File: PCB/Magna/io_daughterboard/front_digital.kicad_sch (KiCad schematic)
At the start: 67 parts, among them U1801 XL9535

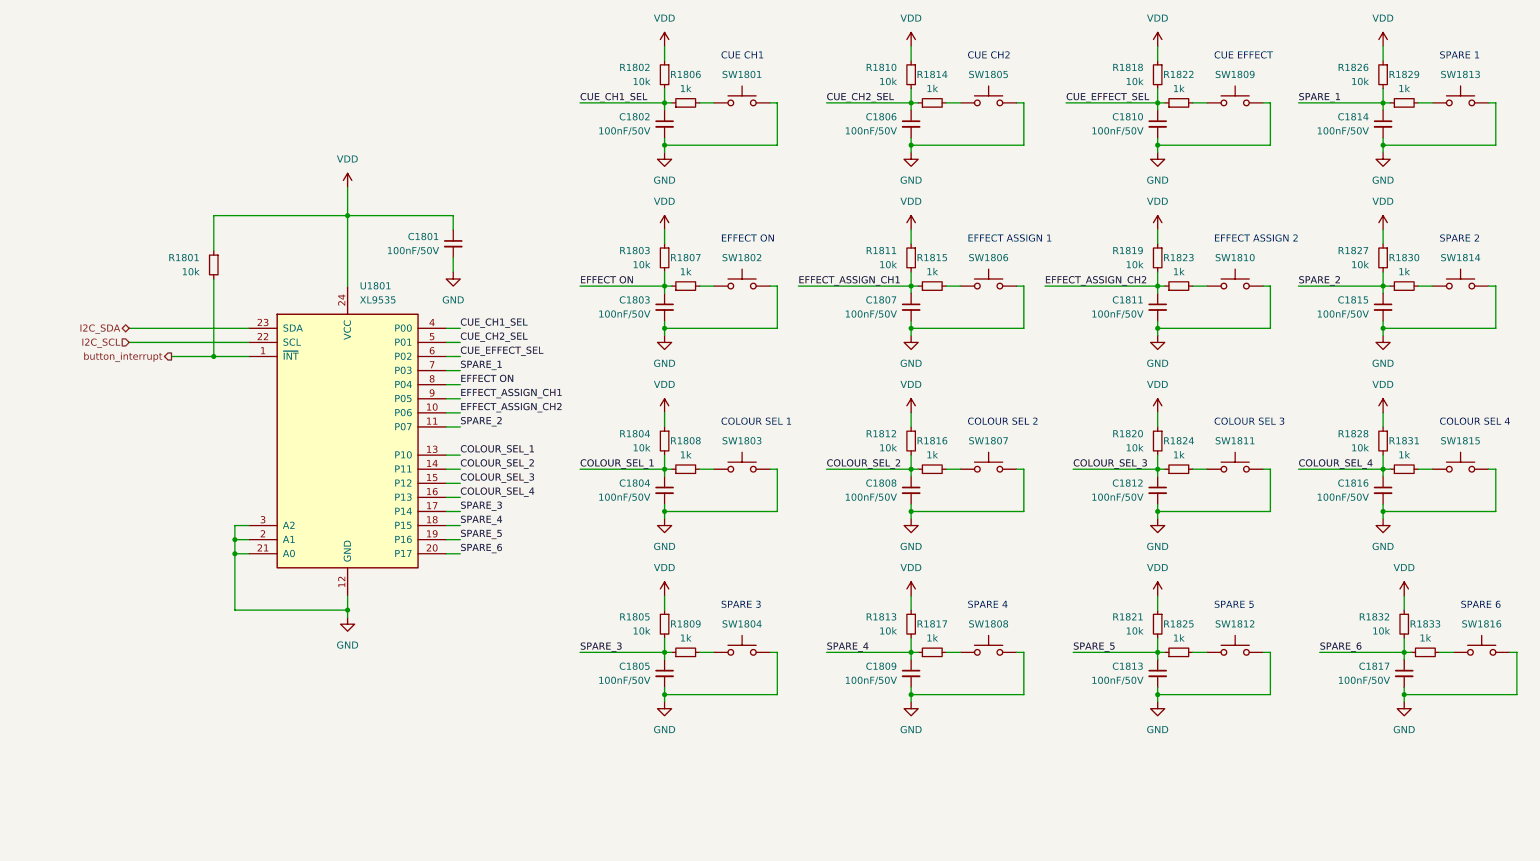
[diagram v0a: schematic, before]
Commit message: Split schematic to several projects
To allow for several boards to be done a kicad project
is needed for each
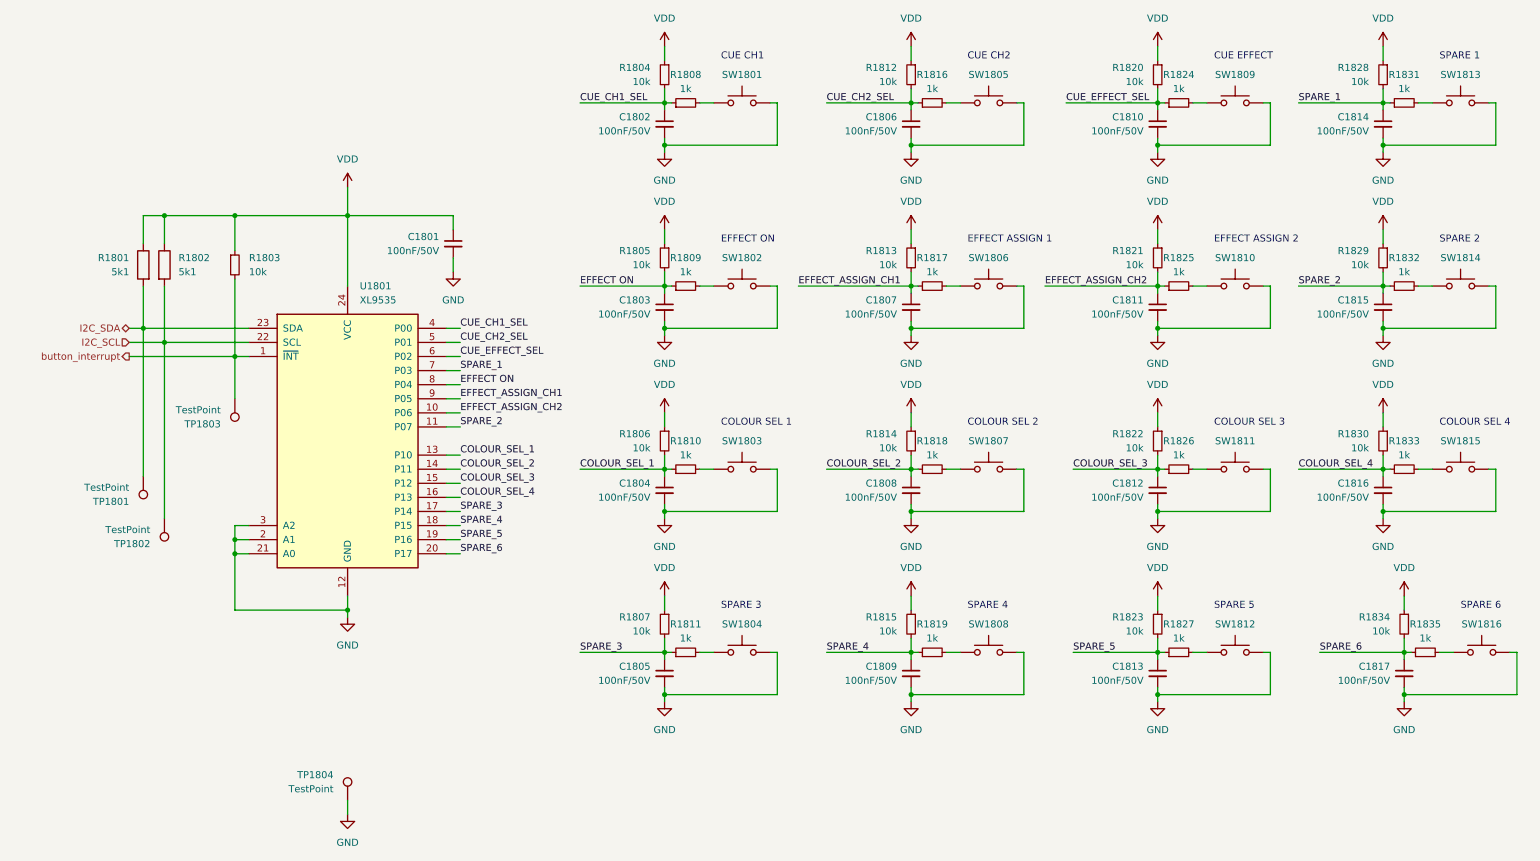
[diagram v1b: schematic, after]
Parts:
- added R1801, R1802: 5k1, Resistor_SMD:R_0805_2012Metric_Pad1.20x1.40mm_HandSolder, symbol Device:R
- added TP1801, TP1802, TP1803, TP1804: TestPoint, TestPoint:TestPoint_Keystone_5005-5009_Compact, symbol Connector:TestPoint
- renumbered R1801 to R1803, R1802 to R1804, R1803 to R1805, R1804 to R1806, R1805 to R1807, R1806 to R1808, R1807 to R1809, R1808 to R1810, R1809 to R1811, R1810 to R1812, R1811 to R1813, R1812 to R1814, R1813 to R1815, R1814 to R1816, R1815 to R1817, R1816 to R1818, R1817 to R1819, R1818 to R1820, R1819 to R1821, R1820 to R1822, R1821 to R1823, R1822 to R1824, R1823 to R1825, R1824 to R1826, R1825 to R1827, R1826 to R1828, R1827 to R1829, R1828 to R1830, R1829 to R1831, R1830 to R1832, R1831 to R1833, R1832 to R1834, R1833 to R1835
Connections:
- net GND: now also TP1804.1
- net I2C_SCL: now also R1802.2, TP1802.1
- net I2C_SDA: now also R1801.2, TP1801.1
- net VDD: now also R1801.1, R1802.1
- net button_interrupt: now also TP1803.1
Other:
- moved on the sheet: R1803

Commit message: Route most of io daughterboard
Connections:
- net COLOUR_SEL_1: no longer U1801.13 (P10)
- net COLOUR_SEL_2: now also U1801.18 (P15); no longer U1801.14 (P11)
- net COLOUR_SEL_3: now also U1801.19 (P16); no longer U1801.15 (P12)
- net COLOUR_SEL_4: now also U1801.20 (P17); no longer U1801.16 (P13)
- net CUE_CH1_SEL: no longer U1801.4 (P00)
- net CUE_CH2_SEL: now also U1801.15 (P12); no longer U1801.5 (P01)
- net CUE_EFFECT_SEL: now also U1801.10 (P06); no longer U1801.6 (P02)
- net EFFECT ON: now also U1801.4 (P00); no longer U1801.8 (P04)
- net EFFECT_ASSIGN_CH1: now also U1801.13 (P10); no longer U1801.9 (P05)
- net EFFECT_ASSIGN_CH2: now also U1801.14 (P11); no longer U1801.10 (P06)
- net SPARE_1: now also U1801.11 (P07); no longer U1801.7 (P03)
- net SPARE_2: now also U1801.9 (P05); no longer U1801.11 (P07)
- net SPARE_3: now also U1801.5 (P01); no longer U1801.17 (P14)
- net SPARE_4: now also U1801.6 (P02); no longer U1801.18 (P15)
- net SPARE_5: now also U1801.7 (P03); no longer U1801.19 (P16)
- net SPARE_6: now also U1801.8 (P04); no longer U1801.20 (P17)
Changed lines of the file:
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@@
   (junction (at 165.1 81.28) (diameter 0) (color 0 0 0 0)
   )
+  (junction (at 120.65 48.26) (diameter 0) (color 0 0 0 0)
+  )
   (junction (at 63.5 60.96) (diameter 0) (color 0 0 0 0)
   )
@@
   (junction (at 209.55 48.26) (diameter 0) (color 0 0 0 0)
   )
-  (junction (at 120.65 48.26) (diameter 0) (color 0 0 0 0)
-  )
   (junction (at 120.65 139.7) (diameter 0) (color 0 0 0 0)
   )
@@
     (stroke (width 0) (type default))
   )
+  (wire (pts (xy 120.65 48.26) (xy 120.65 49.53))
+    (stroke (width 0) (type default))
+  )
   (wire (pts (xy 81.28 104.14) (xy 83.82 104.14))
     (stroke (width 0) (type default))
@@
     (stroke (width 0) (type default))
   )
+  (wire (pts (xy 140.97 48.26) (xy 120.65 48.26))
+    (stroke (width 0) (type default))
+  )
   (wire (pts (xy 234.95 73.66) (xy 250.19 73.66))
     (stroke (width 0) (type default))
@@
     (stroke (width 0) (type default))
   )
-  (wire (pts (xy 140.97 48.26) (xy 140.97 40.64))
-    (stroke (width 0) (type default))
-  )
   (wire (pts (xy 120.65 147.32) (xy 140.97 147.32))
     (stroke (width 0) (type default))
@@
     (stroke (width 0) (type default))
   )
-  (wire (pts (xy 120.65 48.26) (xy 140.97 48.26))
-    (stroke (width 0) (type default))
-  )
   (wire (pts (xy 209.55 114.3) (xy 209.55 115.57))
     (stroke (width 0) (type default))
@@
     (stroke (width 0) (type default))
   )
-  (wire (pts (xy 105.41 40.64) (xy 120.65 40.64))
+  (wire (pts (xy 97.79 40.64) (xy 120.65 40.64))
     (stroke (width 0) (type default))
   )
@@
     (stroke (width 0) (type default))
   )
+  (wire (pts (xy 140.97 40.64) (xy 140.97 48.26))
+    (stroke (width 0) (type default))
+  )
   (wire (pts (xy 166.37 73.66) (xy 165.1 73.66))
     (stroke (width 0) (type default))
@@
     (stroke (width 0) (type default))
   )
-  (wire (pts (xy 120.65 48.26) (xy 120.65 49.53))
-    (stroke (width 0) (type default))
-  )
   (wire (pts (xy 81.28 119.38) (xy 83.82 119.38))
     (stroke (width 0) (type default))
@@
     (effects (font (size 1.27 1.27)) (justify left bottom))
   )
-  (label "EFFECT_ASSIGN_CH2" (at 83.82 96.52 0) (fields_autoplaced)
+  (label "EFFECT_ASSIGN_CH2" (at 83.82 106.68 0) (fields_autoplaced)
     (effects (font (size 1.27 1.27)) (justify left bottom))
   )
-  (label "SPARE_4" (at 83.82 116.84 0) (fields_autoplaced)
+  (label "SPARE_4" (at 83.82 86.36 0) (fields_autoplaced)
     (effects (font (size 1.27 1.27)) (justify left bottom))
   )
@@
     (effects (font (size 1.27 1.27)) (justify left bottom))
   )
-  (label "COLOUR_SEL_4" (at 83.82 111.76 0) (fields_autoplaced)
+  (label "COLOUR_SEL_4" (at 83.82 121.92 0) (fields_autoplaced)
     (effects (font (size 1.27 1.27)) (justify left bottom))
   )
@@
     (effects (font (size 1.27 1.27)) (justify left bottom))
   )
-  (label "SPARE_3" (at 83.82 114.3 0) (fields_autoplaced)
+  (label "SPARE_3" (at 83.82 83.82 0) (fields_autoplaced)
     (effects (font (size 1.27 1.27)) (justify left bottom))
   )
-  (label "CUE_CH2_SEL" (at 83.82 83.82 0) (fields_autoplaced)
+  (label "CUE_CH2_SEL" (at 83.82 109.22 0) (fields_autoplaced)
     (effects (font (size 1.27 1.27)) (justify left bottom))
   )
-  (label "CUE_EFFECT_SEL" (at 83.82 86.36 0) (fields_autoplaced)
+  (label "CUE_EFFECT_SEL" (at 83.82 96.52 0) (fields_autoplaced)
     (effects (font (size 1.27 1.27)) (justify left bottom))
   )
-  (label "EFFECT ON" (at 83.82 91.44 0) (fields_autoplaced)
+  (label "EFFECT ON" (at 83.82 81.28 0) (fields_autoplaced)
     (effects (font (size 1.27 1.27)) (justify left bottom))
   )
@@
     (effects (font (size 1.27 1.27)) (justify left bottom))
   )
-  (label "SPARE_6" (at 83.82 121.92 0) (fields_autoplaced)
+  (label "SPARE_6" (at 83.82 91.44 0) (fields_autoplaced)
     (effects (font (size 1.27 1.27)) (justify left bottom))
   )
@@
     (effects (font (size 1.27 1.27)) (justify left bottom))
   )
-  (label "COLOUR_SEL_1" (at 83.82 104.14 0) (fields_autoplaced)
+  (label "COLOUR_SEL_1" (at 86.36 135.255 0) (fields_autoplaced)
     (effects (font (size 1.27 1.27)) (justify left bottom))
   )
@@
     (effects (font (size 1.27 1.27)) (justify left bottom))
   )
-  (label "COLOUR_SEL_3" (at 83.82 109.22 0) (fields_autoplaced)
+  (label "COLOUR_SEL_3" (at 83.82 119.38 0) (fields_autoplaced)
     (effects (font (size 1.27 1.27)) (justify left bottom))
   )
-  (label "SPARE_1" (at 83.82 88.9 0) (fields_autoplaced)
+  (label "SPARE_1" (at 83.82 99.06 0) (fields_autoplaced)
     (effects (font (size 1.27 1.27)) (justify left bottom))
   )
@@
     (effects (font (size 1.27 1.27)) (justify left bottom))
   )
-  (label "CUE_CH1_SEL" (at 83.82 81.28 0) (fields_autoplaced)
+  (label "CUE_CH1_SEL" (at 90.805 65.405 0) (fields_autoplaced)
     (effects (font (size 1.27 1.27)) (justify left bottom))
   )
-  (label "EFFECT_ASSIGN_CH1" (at 83.82 93.98 0) (fields_autoplaced)
+  (label "EFFECT_ASSIGN_CH1" (at 83.82 104.14 0) (fields_autoplaced)
     (effects (font (size 1.27 1.27)) (justify left bottom))
   )
-  (label "CUE_CH1_SEL" (at 105.41 40.64 0) (fields_autoplaced)
+  (label "CUE_CH1_SEL" (at 97.79 40.64 0) (fields_autoplaced)
     (effects (font (size 1.27 1.27)) (justify left bottom))
   )
-  (label "SPARE_5" (at 83.82 119.38 0) (fields_autoplaced)
+  (label "SPARE_5" (at 83.82 88.9 0) (fields_autoplaced)
     (effects (font (size 1.27 1.27)) (justify left bottom))
   )
-  (label "COLOUR_SEL_2" (at 83.82 106.68 0) (fields_autoplaced)
+  (label "COLOUR_SEL_2" (at 83.82 116.84 0) (fields_autoplaced)
     (effects (font (size 1.27 1.27)) (justify left bottom))
   )
@@
     (effects (font (size 1.27 1.27)) (justify left bottom))
   )
-  (label "SPARE_2" (at 83.82 99.06 0) (fields_autoplaced)
+  (label "SPARE_2" (at 83.82 93.98 0) (fields_autoplaced)
     (effects (font (size 1.27 1.27)) (justify left bottom))
   )
@@
     )
   )
-  (symbol (lib_id "Device:C_Small") (at 120.65 44.45 0) (unit 1)
+  (symbol (lib_id "Device:C_Small") (at 120.65 44.45 0) (mirror y) (unit 1)
     (in_bom yes) (on_board yes) (dnp no)
-    (property "Reference" "C1802" (at 118.11 43.1863 0)
+    (property "Reference" "C1802" (at 123.19 43.1863 0)
       (effects (font (size 1.27 1.27)) (justify right))
     )
-    (property "Value" "100nF/50V" (at 118.11 45.7263 0)
+    (property "Value" "100nF/50V" (at 123.19 45.7263 0)
       (effects (font (size 1.27 1.27)) (justify right))
     )

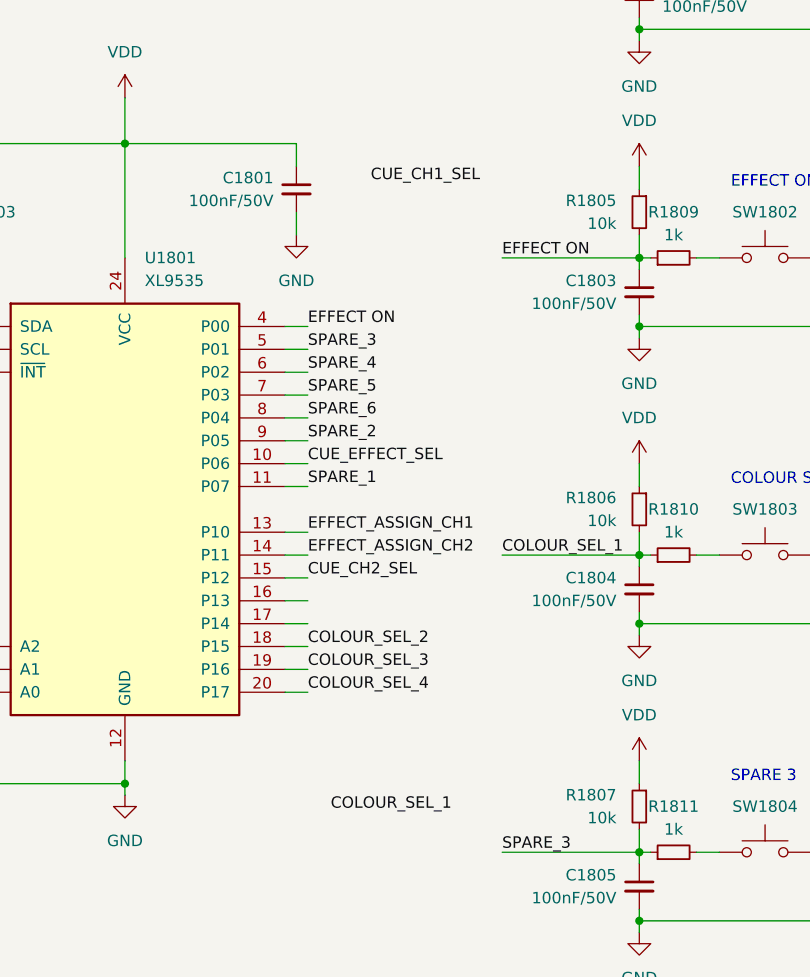
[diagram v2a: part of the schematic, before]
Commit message: Add more routing to IO Daugherboard
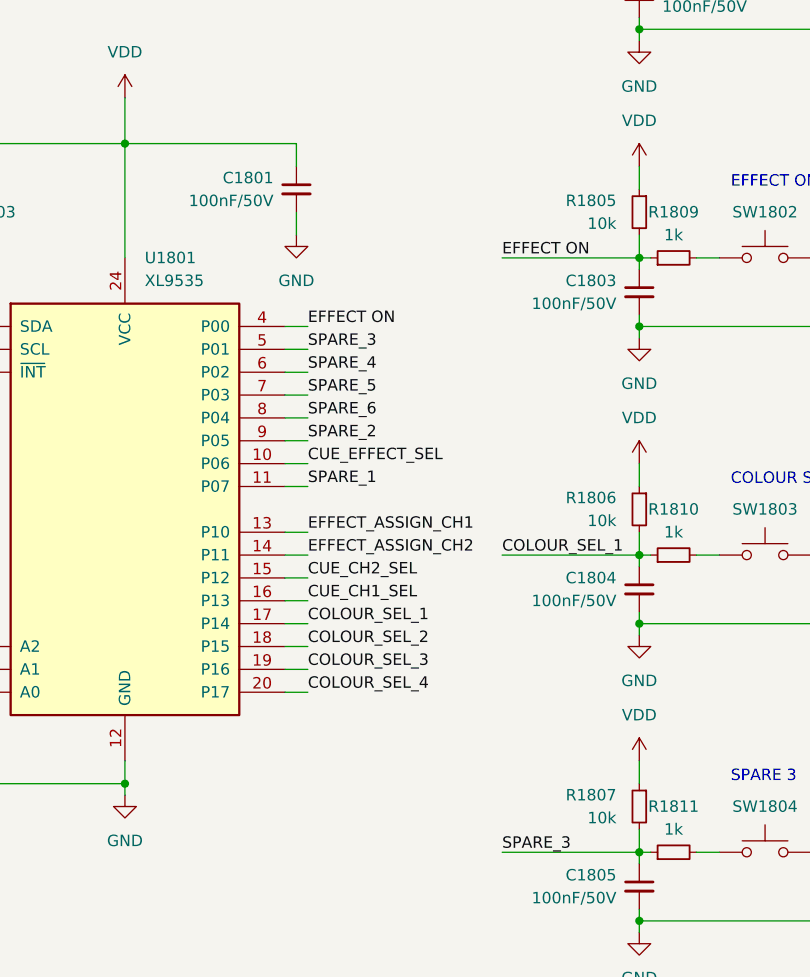
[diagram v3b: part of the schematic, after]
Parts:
- TP1801, TP1802, TP1803, TP1804: footprint TestPoint:TestPoint_Keystone_5005-5009_Compact -> TestPoint:TestPoint_Keystone_5000-5004_Miniature
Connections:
- net COLOUR_SEL_1: now also U1801.17 (P14)
- net CUE_CH1_SEL: now also U1801.16 (P13)
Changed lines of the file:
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@@
     (effects (font (size 1.27 1.27)) (justify left bottom))
   )
+  (label "COLOUR_SEL_1" (at 83.82 114.3 0) (fields_autoplaced)
+    (effects (font (size 1.27 1.27)) (justify left bottom))
+  )
   (label "SPARE_4" (at 149.86 139.7 0) (fields_autoplaced)
     (effects (font (size 1.27 1.27)) (justify left bottom))
@@
     (effects (font (size 1.27 1.27)) (justify left bottom))
   )
-  (label "COLOUR_SEL_1" (at 86.36 135.255 0) (fields_autoplaced)
-    (effects (font (size 1.27 1.27)) (justify left bottom))
-  )
   (label "SPARE_3" (at 105.41 139.7 0) (fields_autoplaced)
     (effects (font (size 1.27 1.27)) (justify left bottom))
@@
     (effects (font (size 1.27 1.27)) (justify left bottom))
   )
-  (label "CUE_CH1_SEL" (at 90.805 65.405 0) (fields_autoplaced)
+  (label "CUE_CH1_SEL" (at 83.82 111.76 0) (fields_autoplaced)
     (effects (font (size 1.27 1.27)) (justify left bottom))
   )
@@
       (effects (font (size 1.27 1.27)) (justify left))
     )
-    (property "Footprint" "TestPoint:TestPoint_Keystone_5005-5009_Compact" (at 21.59 107.95 0)
+    (property "Footprint" "TestPoint:TestPoint_Keystone_5000-5004_Miniature" (at 21.59 107.95 0)
       (effects (font (size 1.27 1.27)) hide)
     )
@@
       (effects (font (size 1.27 1.27)) (justify left))
     )
-    (property "Footprint" "TestPoint:TestPoint_Keystone_5005-5009_Compact" (at 25.4 115.57 0)
+    (property "Footprint" "TestPoint:TestPoint_Keystone_5000-5004_Miniature" (at 25.4 115.57 0)
       (effects (font (size 1.27 1.27)) hide)
     )
@@
       (effects (font (size 1.27 1.27)) (justify left))
     )
-    (property "Footprint" "TestPoint:TestPoint_Keystone_5005-5009_Compact" (at 38.1 93.98 0)
+    (property "Footprint" "TestPoint:TestPoint_Keystone_5000-5004_Miniature" (at 38.1 93.98 0)
       (effects (font (size 1.27 1.27)) hide)
     )
@@
       (effects (font (size 1.27 1.27)) (justify right))
     )
-    (property "Footprint" "TestPoint:TestPoint_Keystone_5005-5009_Compact" (at 68.58 166.37 0)
+    (property "Footprint" "TestPoint:TestPoint_Keystone_5000-5004_Miniature" (at 68.58 166.37 0)
       (effects (font (size 1.27 1.27)) hide)
     )

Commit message: Make IO daughterboard production ready
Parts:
- SW1801, SW1802, SW1803, SW1804, SW1805, SW1806, SW1807, SW1808, SW1809, SW1810, SW1811, SW1812, SW1813, SW1814, SW1815, SW1816: LCSC (none) -> C318884
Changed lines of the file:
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@@
+      (effects (font (size 1.27 1.27)) hide)
+    )
+    (property "LCSC" "C318884" (at 134.62 139.7 0)
       (effects (font (size 1.27 1.27)) hide)
     )
@@
       (effects (font (size 1.27 1.27)) hide)
     )
+    (property "LCSC" "C318884" (at 179.07 73.66 0)
+      (effects (font (size 1.27 1.27)) hide)
+    )
     (pin "2")
     (pin "1")
@@
     )
     (property "Datasheet" "~" (at 264.16 68.58 0)
+      (effects (font (size 1.27 1.27)) hide)
+    )
+    (property "LCSC" "C318884" (at 264.16 73.66 0)
       (effects (font (size 1.27 1.27)) hide)
     )
@@
       (effects (font (size 1.27 1.27)) hide)
     )
+    (property "LCSC" "C318884" (at 223.52 139.7 0)
+      (effects (font (size 1.27 1.27)) hide)
+    )
     (pin "2")
     (pin "1")
@@
     )
     (property "Datasheet" "~" (at 223.52 35.56 0)
+      (effects (font (size 1.27 1.27)) hide)
+    )
+    (property "LCSC" "C318884" (at 223.52 40.64 0)
       (effects (font (size 1.27 1.27)) hide)
     )
@@
       (effects (font (size 1.27 1.27)) hide)
     )
+    (property "LCSC" "C318884" (at 134.62 73.66 0)
+      (effects (font (size 1.27 1.27)) hide)
+    )
     (pin "2")
     (pin "1")
@@
     )
     (property "Datasheet" "~" (at 223.52 101.6 0)
+      (effects (font (size 1.27 1.27)) hide)
+    )
+    (property "LCSC" "C318884" (at 223.52 106.68 0)
       (effects (font (size 1.27 1.27)) hide)
     )
@@
       (effects (font (size 1.27 1.27)) hide)
     )
+    (property "LCSC" "C318884" (at 179.07 40.64 0)
+      (effects (font (size 1.27 1.27)) hide)
+    )
     (pin "2")
     (pin "1")
@@
       (effects (font (size 1.27 1.27)) hide)
     )
+    (property "LCSC" "C318884" (at 267.97 139.7 0)
+      (effects (font (size 1.27 1.27)) hide)
+    )
     (pin "2")
     (pin "1")
@@
       (effects (font (size 1.27 1.27)) hide)
     )
+    (property "LCSC" "C318884" (at 134.62 40.64 0)
+      (effects (font (size 1.27 1.27)) hide)
+    )
     (pin "2")
     (pin "1")
@@
       (effects (font (size 1.27 1.27)) hide)
     )
+    (property "LCSC" "C318884" (at 179.07 106.68 0)
+      (effects (font (size 1.27 1.27)) hide)
+    )
     (pin "2")
     (pin "1")
@@
     )
     (property "Datasheet" "~" (at 264.16 101.6 0)
+      (effects (font (size 1.27 1.27)) hide)
+    )
+    (property "LCSC" "C318884" (at 264.16 106.68 0)
       (effects (font (size 1.27 1.27)) hide)
     )
@@
       (effects (font (size 1.27 1.27)) hide)
     )
+    (property "LCSC" "C318884" (at 134.62 106.68 0)
+      (effects (font (size 1.27 1.27)) hide)
+    )
     (pin "2")
     (pin "1")
@@
     )
     (property "Datasheet" "~" (at 223.52 68.58 0)
+      (effects (font (size 1.27 1.27)) hide)
+    )
+    (property "LCSC" "C318884" (at 223.52 73.66 0)
       (effects (font (size 1.27 1.27)) hide)
     )
@@
       (effects (font (size 1.27 1.27)) hide)
     )
+    (property "LCSC" "C318884" (at 179.07 139.7 0)
+      (effects (font (size 1.27 1.27)) hide)
+    )
     (pin "2")
     (pin "1")
@@
       (effects (font (size 1.27 1.27)) hide)
     )
+    (property "LCSC" "C318884" (at 264.16 40.64 0)
+      (effects (font (size 1.27 1.27)) hide)
+    )
